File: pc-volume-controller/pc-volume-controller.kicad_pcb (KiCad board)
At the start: 2 copper layers, 98 x 54 mm, 16 parts, among them U1 Arduino_Nano_v3.x

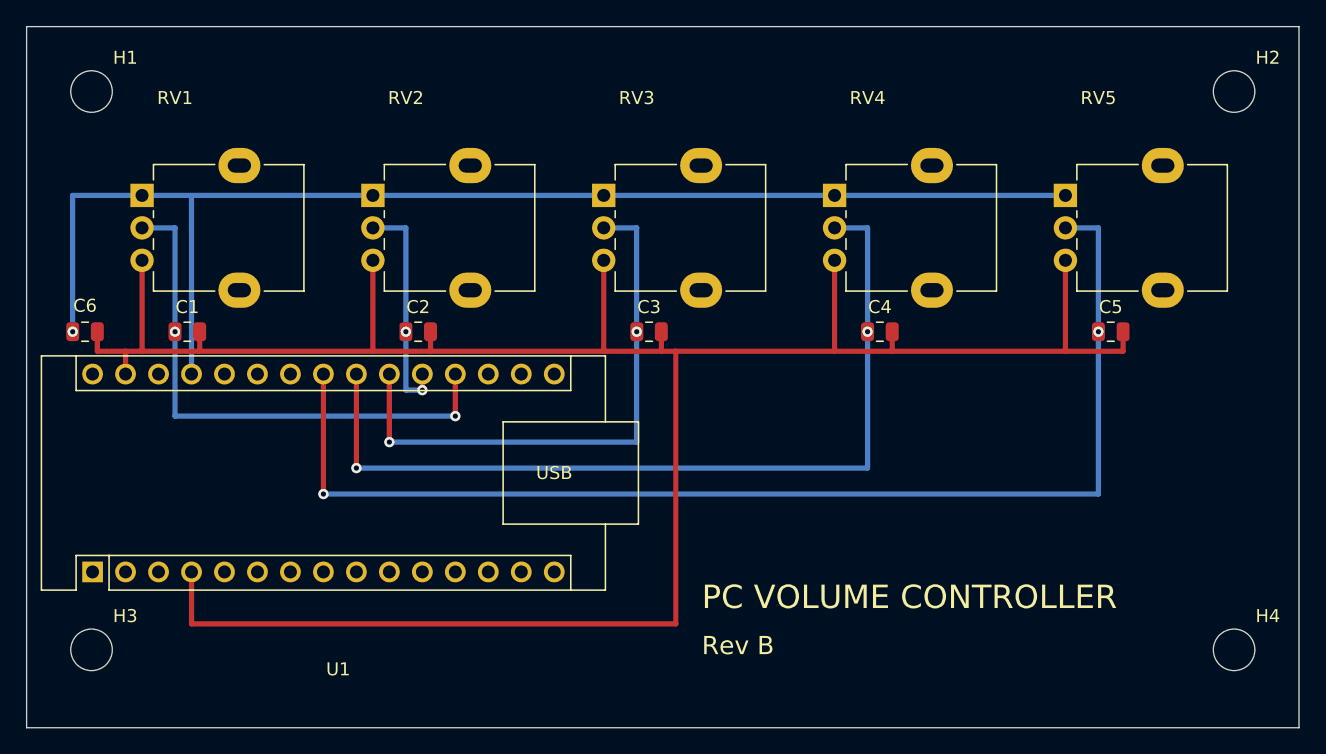
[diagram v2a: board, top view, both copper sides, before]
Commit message: Apply EMC/DFM review fixes: ground plane, stitching, fiducials, return paths
Board was run through a design review (schematic, PCB, EMC, cross-analysis).
Four findings fixed and independently re-verified:

- GP-002 / VS-002 (no ground plane, no stitching): GND pours on both F.Cu and
  B.Cu -- 0.5 mm edge inset, 0.25 mm clearance, thermal reliefs -- plus 36
  ground stitching vias.
- VP-001 (via in pad x6): the six in-pad vias moved off the C1-C6 pads from
  y=23.50 to y=21.50 and stubbed back with a 0.4 mm F.Cu trace. Topped vias
  wick solder under JLCPCB's standard process.
- FD-001 (no fiducials): three Fiducial_1mm_Mask2mm on F.Cu at (14,50.5),
  (84,50.5), (94,34).
- RP-001 (return path): a 0.6 mm ground via within 0.95 mm of each of the ten
  /VOL* signal layer transitions, closing the return path at every layer change.

Verified after the change:
  DRC   1 violation (pre-existing cosmetic lib_footprint_mismatch on U1)
        0 unconnected items, 0 schematic-parity differences
  ERC   0 violations
  EMC   pre-compliance score 86.5 -> 95.5

make_jlcpcb_outputs.py now intersects the CPL against the BOM designator set
and reports what it dropped. Fiducials are placed but not assembled, and
JLCPCB's PCBA upload rejects a CPL containing orphan designators -- without
this the upload fails with an unhelpful error.

Gerbers, drill, BOM and CPL regenerated from the updated board. The
kicad_pro diff is KiCad materialising its previously-implicit defaults block;
the netclass (clearance 0.2, track 0.2, via 0.6/0.3) is unchanged.
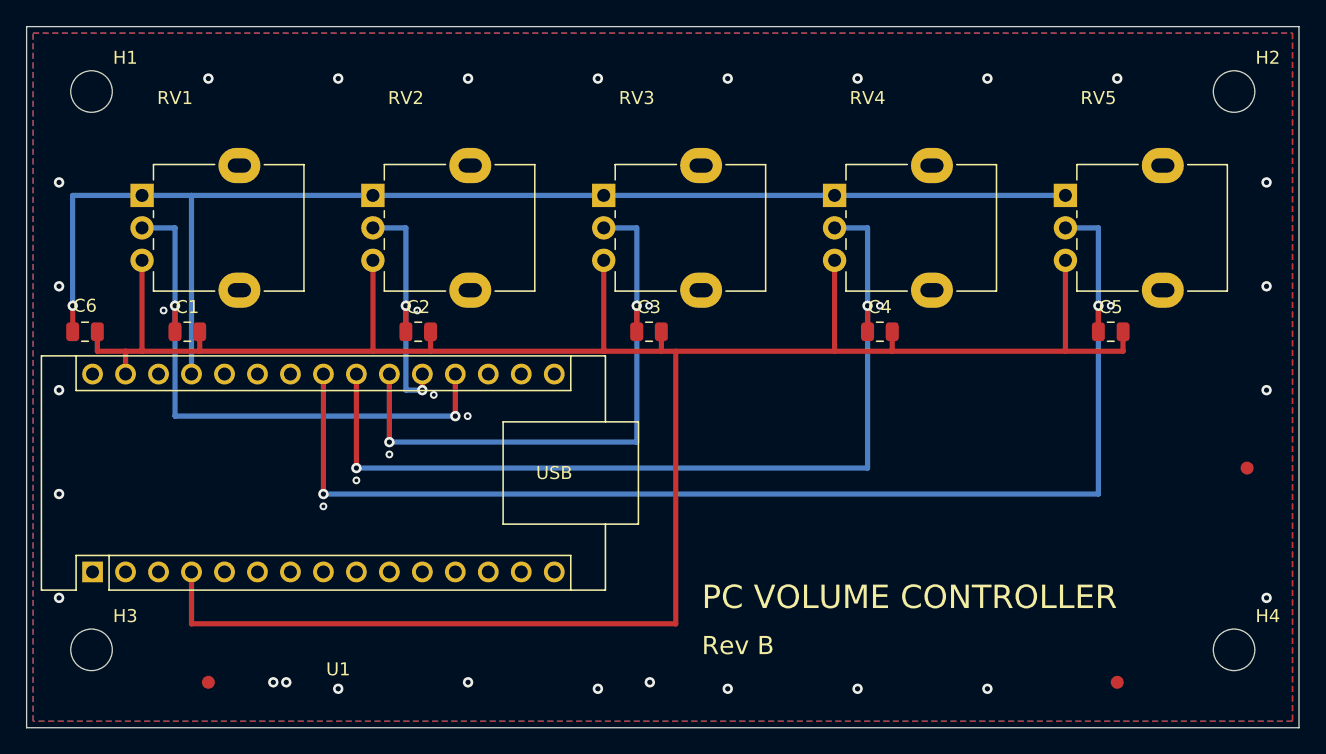
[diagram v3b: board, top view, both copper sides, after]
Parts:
- added FID1: Fiducial_1mm_Mask2mm, Fiducial_1mm_Mask2mm, F.Cu at (14.0, 50.5)
- added FID2: Fiducial_1mm_Mask2mm, Fiducial_1mm_Mask2mm, F.Cu at (84.0, 50.5)
- added FID3: Fiducial_1mm_Mask2mm, Fiducial_1mm_Mask2mm, F.Cu at (94.0, 34.0)
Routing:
- net /VOL5: track 92.0 -> 94.0 mm
- net /VOL4: track 67.6 -> 69.6 mm
- net /VOL3: track 43.3 -> 45.3 mm
- net /VOL2: track 17.5 -> 19.5 mm
- net /VOL1: track 41.9 -> 43.9 mm
- net GND: vias 0 -> 36
- added copper zone on B.Cu, net GND
- added copper zone on F.Cu, net GND
